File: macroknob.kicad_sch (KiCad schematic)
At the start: 8 parts, among them J1 Conn_01x02_Socket, SW1 RotaryEncoder_Switch, U1 Nice_Nano_V2

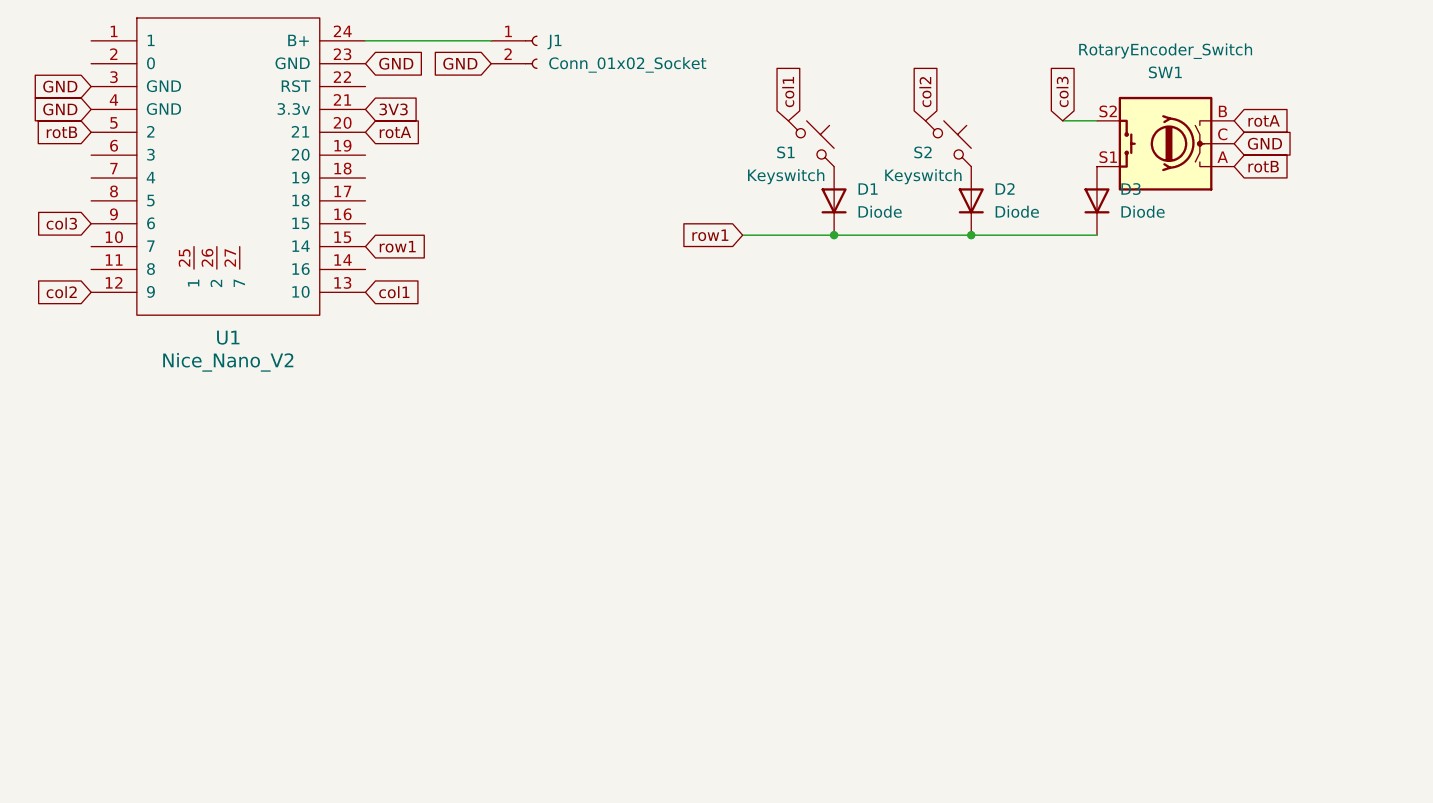
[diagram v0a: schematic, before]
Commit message: Add V3 and case stl
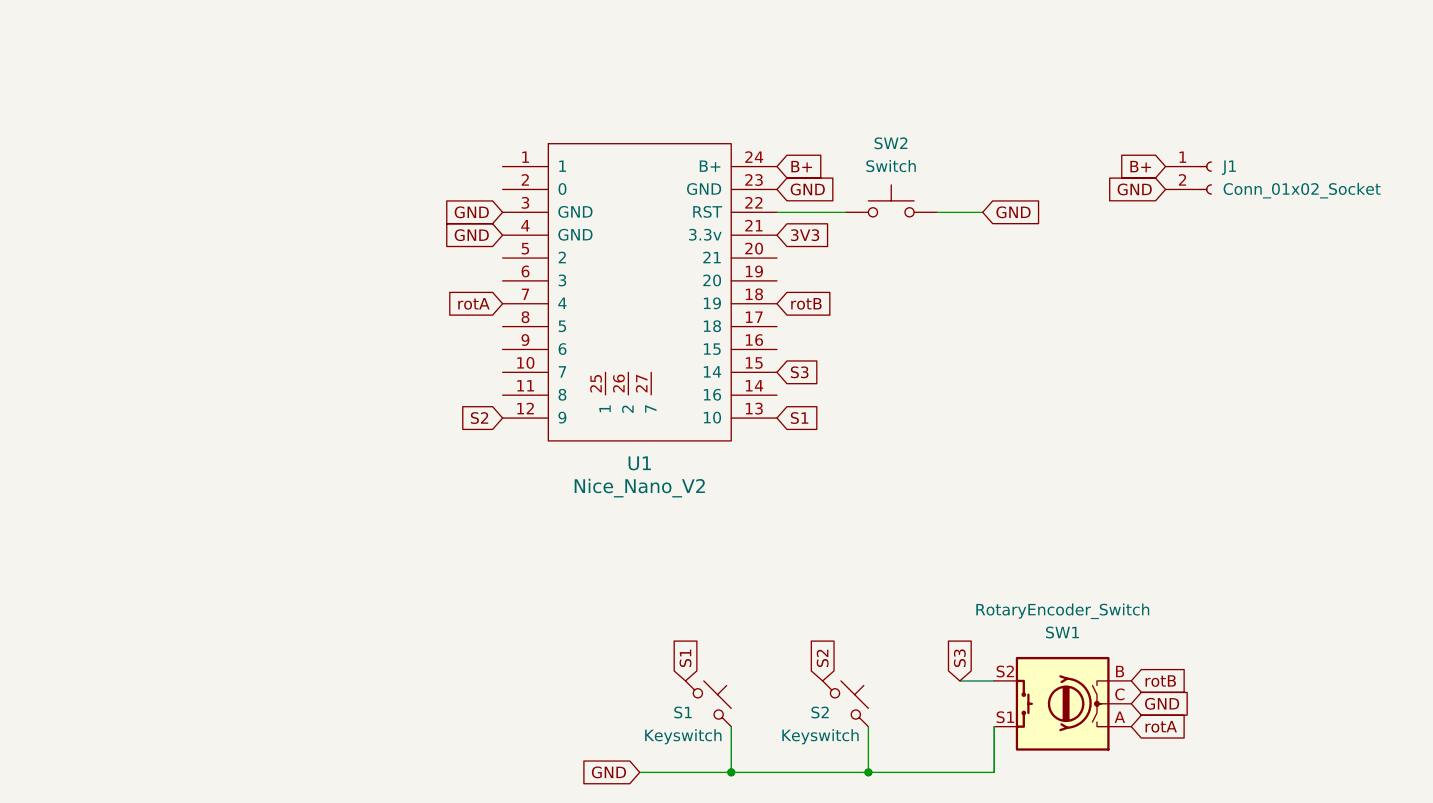
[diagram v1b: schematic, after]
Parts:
- removed D1, D2, D3: Diode, ScottoKeebs_Components:Diode_SOD-123, symbol ScottoKeebs:Placeholder_Diode
- added SW2: Switch, Button_Switch_SMD:SW_SPST_PTS810, symbol ScottoKeebs:Placeholder_Switch
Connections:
- net GND: now also S1.2, S2.2, SW1.S1, SW2.2
- net rotA: now also SW1.A, U1.7 (4); no longer SW1.B, U1.20 (21)
- net rotB: now also SW1.B, U1.18 (19); no longer SW1.A, U1.5 (2)
- net B+: now reaches J1.1 (Pin_1), U1.24 (B+)
- net at U1.22 (RST): now also SW2.1
- net col1 renamed S1
- net col2 renamed S2
- net col3: no longer names the net of U1.9 (6)
- net col3: no longer SW1.S2
- net row1 renamed S3
- net S3: now also SW1.S2
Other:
- moved on the sheet: J1, S1, S2, SW1, U1
